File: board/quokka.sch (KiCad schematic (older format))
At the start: 0 parts

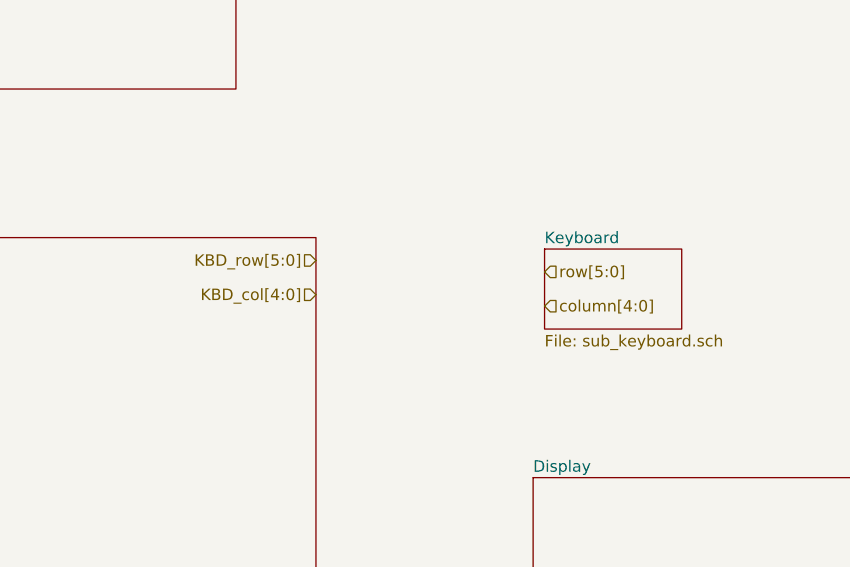
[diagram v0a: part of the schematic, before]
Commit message: Added some buttons
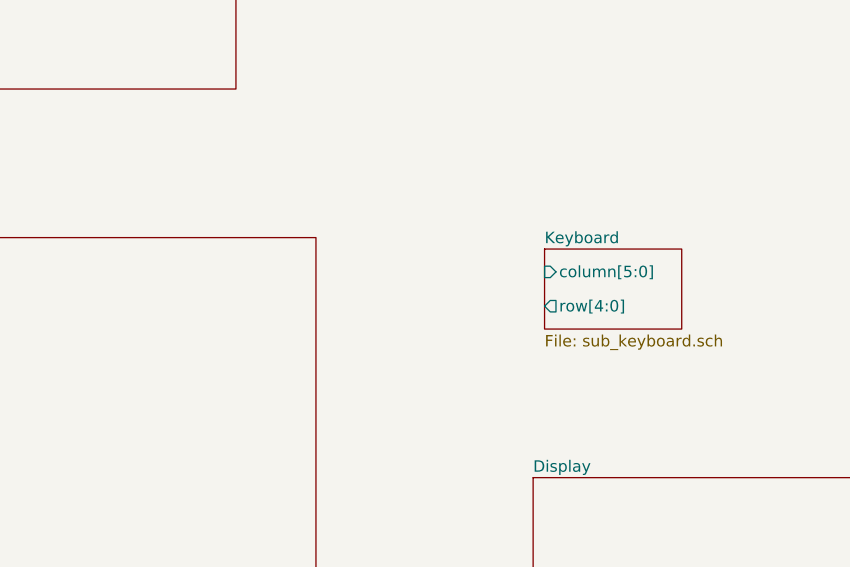
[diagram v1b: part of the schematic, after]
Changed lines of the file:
@@
 EESchema Schematic File Version 4
+LIBS:quokka-cache
 EELAYER 26 0
 EELAYER END
 $Descr A4 11693 8268
 encoding utf-8
-Sheet 1 7
+Sheet 1 8
 Title ""
 Date ""
@@
 F0 "Keyboard" 50
 F1 "sub_keyboard.sch" 50
+F2 "column[5:0]" I L 8400 3750 50
+F3 "row[4:0]" O L 8400 3900 50
 $EndSheet
-Text HLabel 8400 3750 2    50   Input ~ 0
-row[5:0]
-Text HLabel 8400 3900 2    50   Input ~ 0
-column[4:0]
-Text HLabel 7400 3700 0    50   Input ~ 0
-KBD_row[5:0]
-Text HLabel 7400 3850 0    50   Input ~ 0
-KBD_col[4:0]
 $EndSCHEMATC

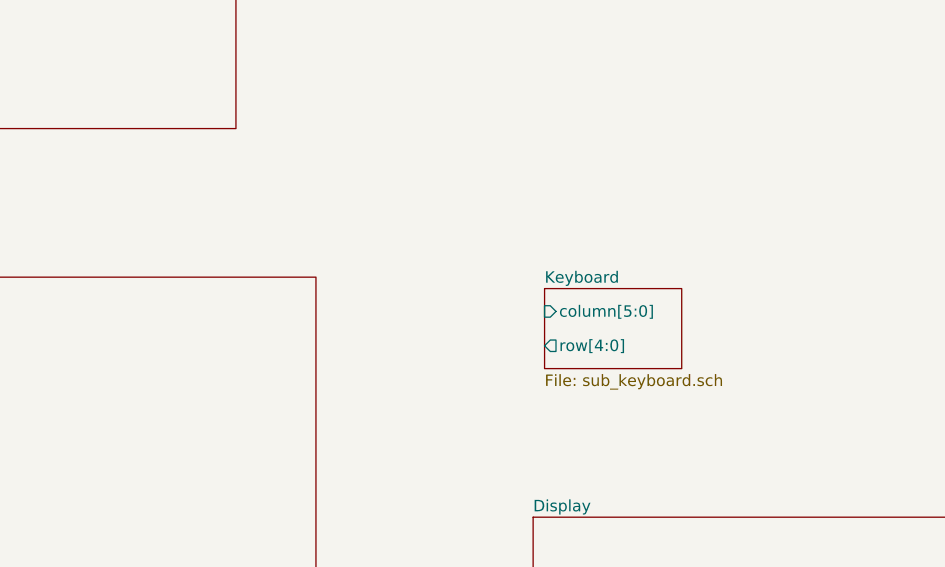
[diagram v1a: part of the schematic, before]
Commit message: Updated keyboard
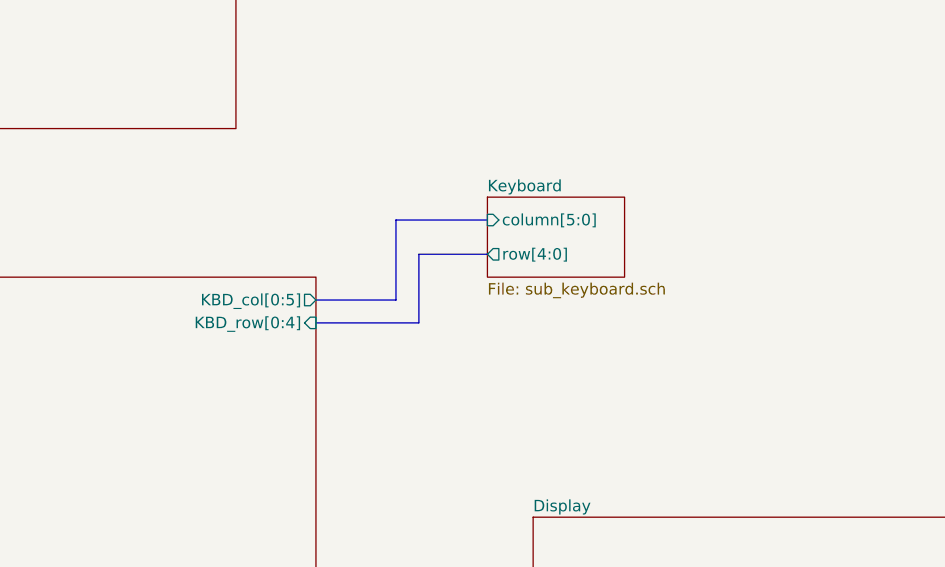
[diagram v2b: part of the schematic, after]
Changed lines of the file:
@@
 F0 "FPGA" 50
 F1 "sub_fpga.sch" 50
+F2 "KBD_col[0:5]" O R 7400 3700 50
+F3 "KBD_row[0:4]" I R 7400 3800 50
 $EndSheet
 $Sheet
@@
 $EndSheet
 $Sheet
-S 8400 3650 600  350
+S 8150 3250 600  350
 U 5A9C1519
 F0 "Keyboard" 50
 F1 "sub_keyboard.sch" 50
-F2 "column[5:0]" I L 8400 3750 50
-F3 "row[4:0]" O L 8400 3900 50
+F2 "column[5:0]" I L 8150 3350 50
+F3 "row[4:0]" O L 8150 3500 50
 $EndSheet
+Wire Bus Line
+	7400 3700 7750 3700
+Wire Bus Line
+	7750 3700 7750 3350
+Wire Bus Line
+	7750 3350 8150 3350
+Wire Bus Line
+	7850 3500 7850 3800
+Wire Bus Line
+	7850 3800 7400 3800
+Wire Bus Line
+	8150 3500 7850 3500
 $EndSCHEMATC

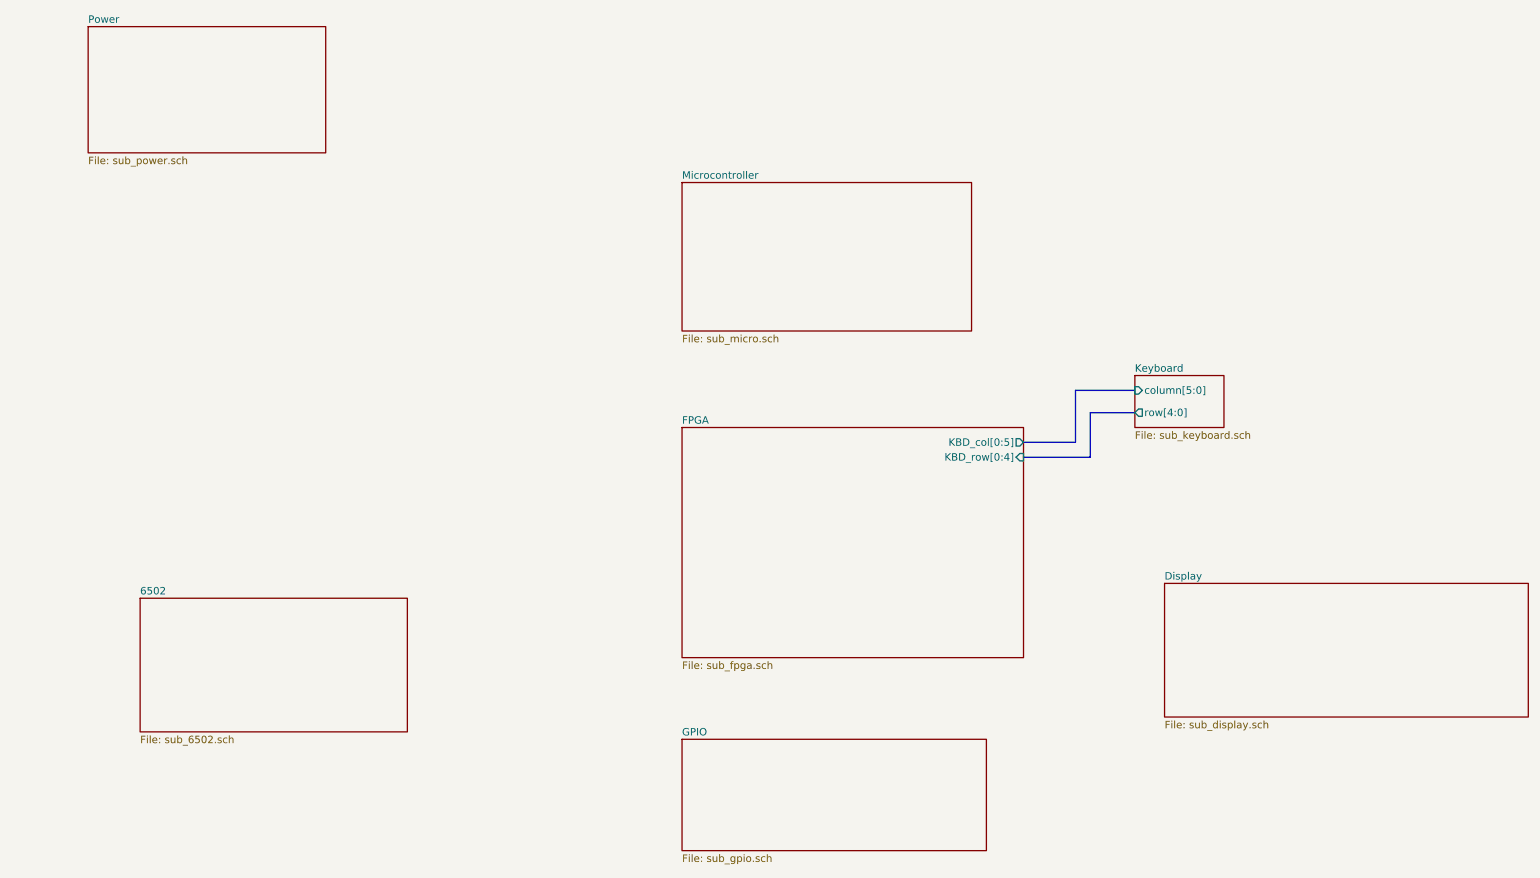
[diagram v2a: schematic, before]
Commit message: More progress on the schematic. 6502 Done.
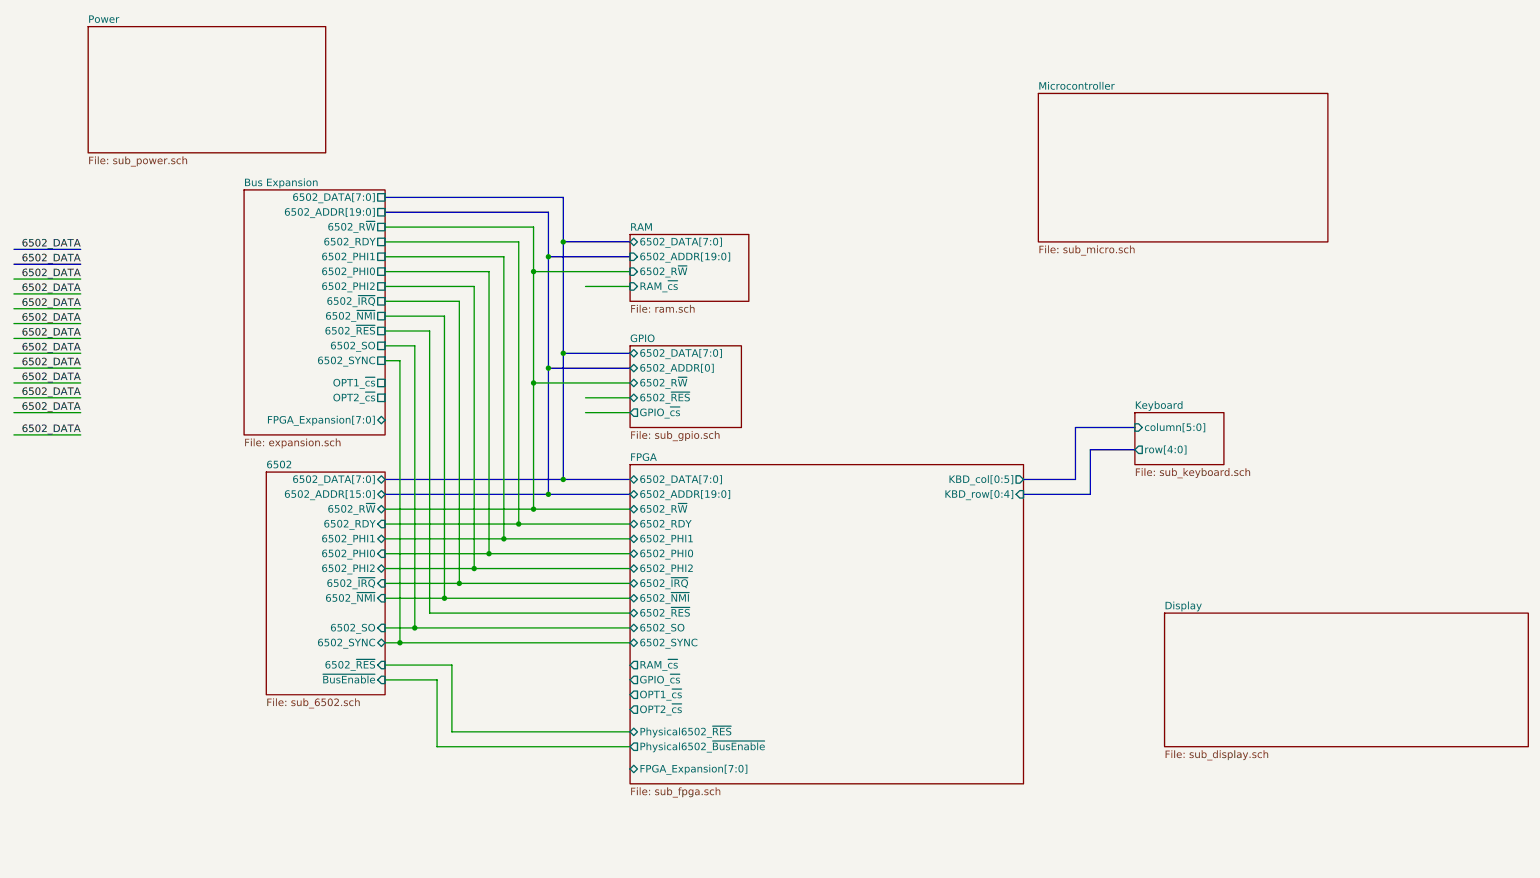
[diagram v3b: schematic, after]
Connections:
- net labels added: 6502_DATA
- wire segments 0 -> 63

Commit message: More schematic progress
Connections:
- net labels removed: 6502_DATA
- wire segments 63 -> 57

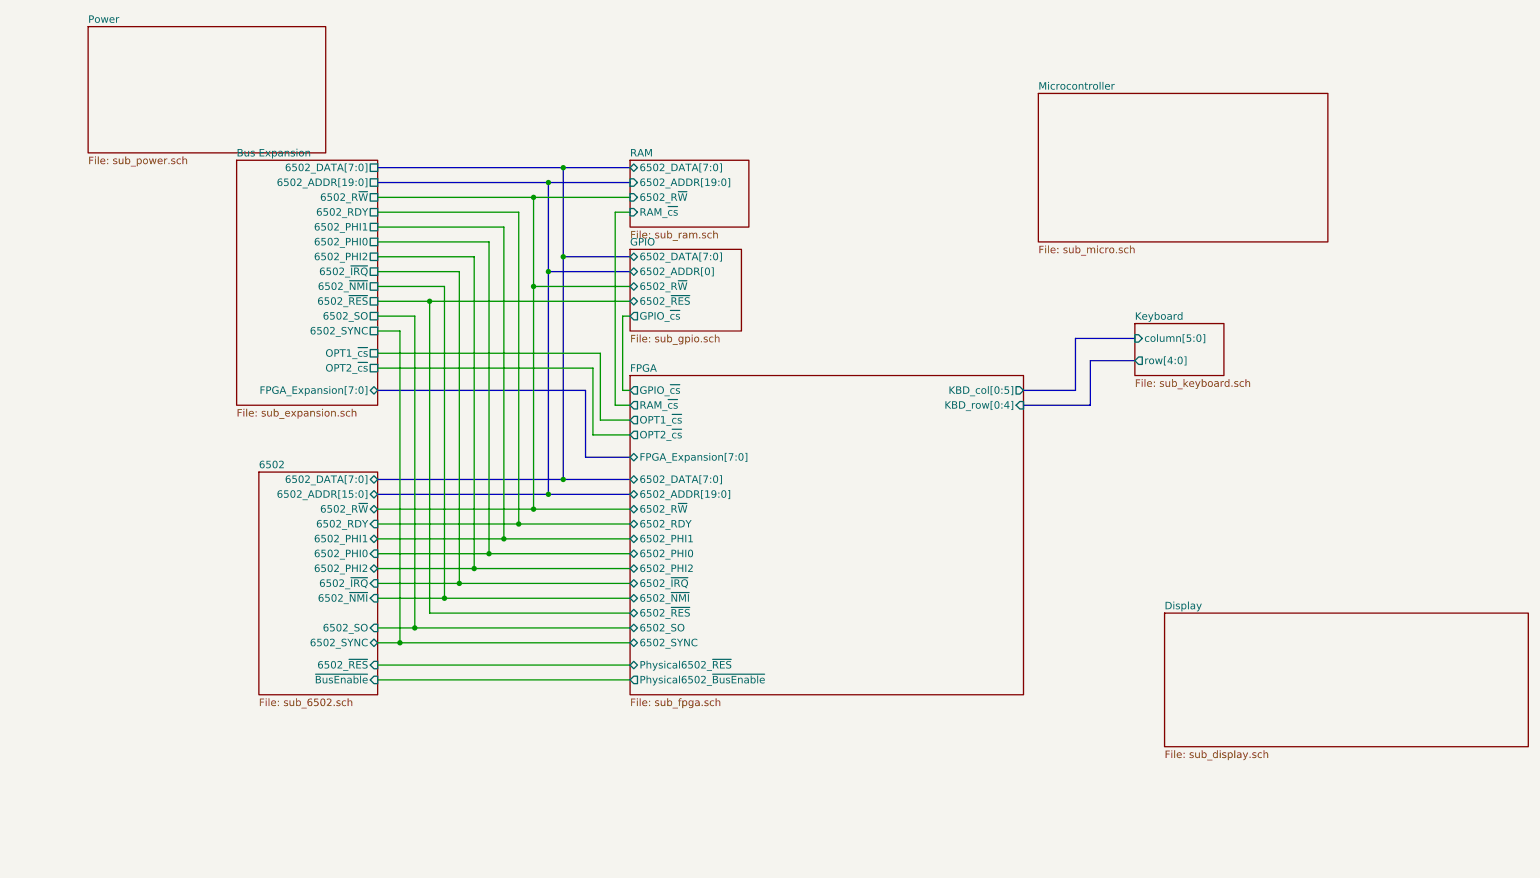
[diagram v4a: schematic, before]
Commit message: Level converters complete, display almost done
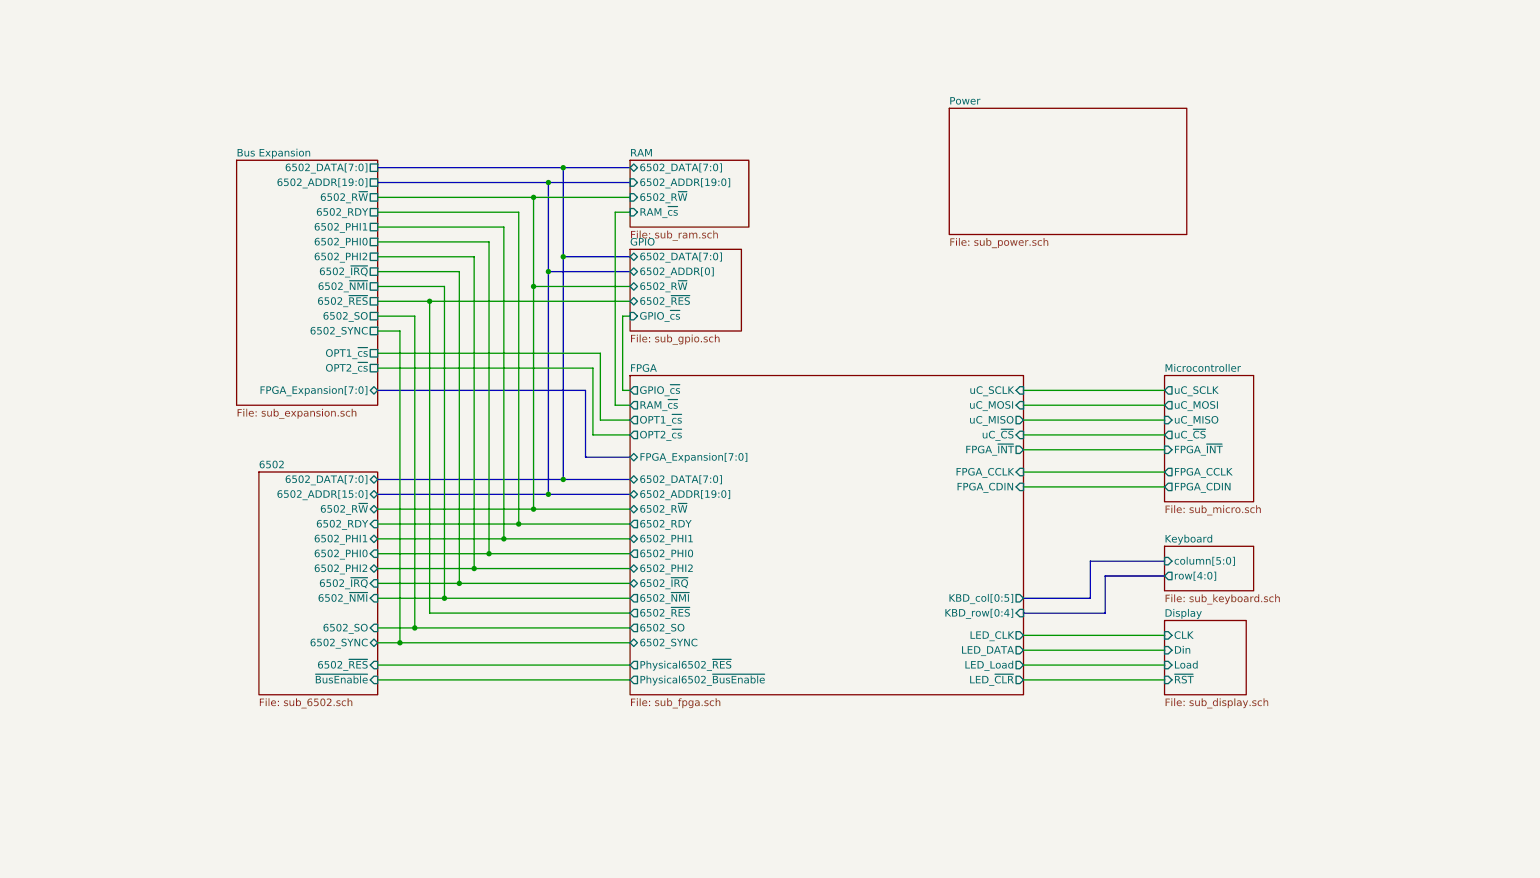
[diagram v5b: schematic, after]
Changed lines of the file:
@@
 EELAYER 26 0
 EELAYER END
-$Descr A4 11693 8268
+$Descr USLetter 11000 8500
 encoding utf-8
-Sheet 1 10
+Sheet 1 15
 Title ""
 Date ""
@@
 Comment2 ""
 Comment3 ""
-Comment4 ""
+Comment4 "Quokka 6502 Microprocessor Trainer"
 $EndDescr
 $Sheet
-S 1100 900  1600 850
+S 6900 1450 1600 850
 U 5A9C14CE
 F0 "Power" 50
@@
 $EndSheet
 $Sheet
-S 7500 1350 1950 1000
+S 8350 3250 600  850
 U 5A9C14E5
 F0 "Microcontroller" 50
 F1 "sub_micro.sch" 50
+F2 "uC_SCLK" O L 8350 3350 50
+F3 "uC_MOSI" O L 8350 3450 50
+F4 "uC_MISO" I L 8350 3550 50
+F5 "uC_~CS" O L 8350 3650 50
+F6 "FPGA_~INT" I L 8350 3750 50
+F7 "FPGA_CCLK" O L 8350 3900 50
+F8 "FPGA_CDIN" O L 8350 4000 50
 $EndSheet
 $Sheet
@@
 F3 "6502_R~W" B L 4750 2650 50
 F4 "6502_ADDR[0]" B L 4750 2550 50
-F5 "GPIO_~cs" O L 4750 2850 50
+F5 "GPIO_~cs" I L 4750 2850 50
 F6 "6502_~RES" B L 4750 2750 50
 $EndSheet
 $Sheet
-S 8350 4850 2450 900
+S 8350 4900 550  500
 U 5A9C150A
 F0 "Display" 50
 F1 "sub_display.sch" 50
-$EndSheet
-$Sheet
-S 8150 2900 600  350
+F2 "CLK" I L 8350 5000 50
+F3 "~RST" I L 8350 5300 50
+F4 "Load" I L 8350 5200 50
+F5 "Din" I L 8350 5100 50
+$EndSheet
+$Sheet
+S 8350 4400 600  300
 U 5A9C1519
 F0 "Keyboard" 50
 F1 "sub_keyboard.sch" 50
-F2 "column[5:0]" I L 8150 3000 50
-F3 "row[4:0]" O L 8150 3150 50
-$EndSheet
-Wire Bus Line
-	7400 3350 7750 3350
-Wire Bus Line
-	7750 3350 7750 3000
-Wire Bus Line
-	7750 3000 8150 3000
-Wire Bus Line
-	7850 3150 7850 3450
-Wire Bus Line
-	7850 3450 7400 3450
-Wire Bus Line
-	8150 3150 7850 3150
+F2 "column[5:0]" I L 8350 4500 50
+F3 "row[4:0]" O L 8350 4600 50
+$EndSheet
 $Sheet
 S 2100 1800 950  1650
@@
 $EndSheet
 $Sheet
-S 4750 3250 2650 2150
-U 5A9C14F1
-F0 "FPGA" 50
-F1 "sub_fpga.sch" 50
-F2 "KBD_col[0:5]" O R 7400 3350 50
-F3 "KBD_row[0:4]" I R 7400 3450 50
-F4 "6502_DATA[7:0]" T L 4750 3950 50
-F5 "6502_RDY" B L 4750 4250 50
-F6 "6502_PHI1" B L 4750 4350 50
-F7 "6502_PHI0" B L 4750 4450 50
-F8 "6502_PHI2" B L 4750 4550 50
-F9 "6502_SO" B L 4750 4950 50
-F10 "6502_ADDR[19:0]" B L 4750 4050 50
-F11 "6502_R~W" B L 4750 4150 50
-F12 "6502_~IRQ" B L 4750 4650 50
-F13 "6502_~NMI" B L 4750 4750 50
-F14 "6502_~RES" B L 4750 4850 50
-F15 "RAM_~cs" O L 4750 3450 50
-F16 "GPIO_~cs" O L 4750 3350 50
-F17 "OPT1_~cs" O L 4750 3550 50
-F18 "OPT2_~cs" O L 4750 3650 50
-F19 "6502_SYNC" B L 4750 5050 50
-F20 "Physical6502_~RES" B L 4750 5200 50
-F21 "Physical6502_~BusEnable" O L 4750 5300 50
-F22 "FPGA_Expansion[7:0]" B L 4750 3800 50
-$EndSheet
-$Sheet
 S 2250 3900 800  1500
 U 5A9C14D9
@@
 Wire Bus Line
 	3050 3350 4450 3350
+$Sheet
+S 4750 3250 2650 2150
+U 5A9C14F1
+F0 "FPGA" 50
+F1 "sub_fpga.sch" 50
+F2 "KBD_col[0:5]" O R 7400 4750 50
+F3 "KBD_row[0:4]" I R 7400 4850 50
+F4 "6502_DATA[7:0]" T L 4750 3950 50
+F5 "6502_ADDR[19:0]" B L 4750 4050 50
+F6 "RAM_~cs" O L 4750 3450 50
+F7 "GPIO_~cs" O L 4750 3350 50
+F8 "OPT1_~cs" O L 4750 3550 50
+F9 "OPT2_~cs" O L 4750 3650 50
+F10 "FPGA_Expansion[7:0]" B L 4750 3800 50
+F11 "LED_CLK" O R 7400 5000 50
+F12 "LED_DATA" O R 7400 5100 50
+F13 "LED_Load" O R 7400 5200 50
+F14 "6502_R~W" B L 4750 4150 50
+F15 "6502_RDY" O L 4750 4250 50
+F16 "6502_PHI1" B L 4750 4350 50
+F17 "6502_PHI0" O L 4750 4450 50
+F18 "6502_PHI2" B L 4750 4550 50
+F19 "6502_~IRQ" B L 4750 4650 50
+F20 "6502_~NMI" O L 4750 4750 50
+F21 "Physical6502_~RES" O L 4750 5200 50
+F22 "6502_SO" O L 4750 4950 50
+F23 "6502_SYNC" B L 4750 5050 50
+F24 "6502_~RES" O L 4750 4850 50
+F25 "Physical6502_~BusEnable" O L 4750 5300 50
+F26 "uC_SCLK" I R 7400 3350 50
+F27 "uC_MOSI" I R 7400 3450 50
+F28 "uC_MISO" O R 7400 3550 50
+F29 "uC_~CS" I R 7400 3650 50
+F30 "FPGA_~INT" O R 7400 3750 50
+F31 "FPGA_CCLK" I R 7400 3900 50
+F32 "FPGA_CDIN" I R 7400 4000 50
+F33 "LED_~CLR" O R 7400 5300 50
+$EndSheet
+Wire Wire Line
+	8350 3350 7400 3350
+Wire Wire Line
+	7400 3450 8350 3450
+Wire Wire Line
+	8350 3550 7400 3550
+Wire Wire Line
+	7400 3650 8350 3650
+Wire Wire Line
+	8350 3750 7400 3750
+Wire Wire Line
+	7400 3900 8350 3900
+Wire Wire Line
+	8350 4000 7400 4000
+Wire Bus Line
+	7950 4600 7950 4850
+Wire Bus Line
+	7950 4850 7400 4850
+Wire Bus Line
+	7950 4600 8350 4600
+Wire Bus Line
+	7400 4750 7850 4750
+Wire Bus Line
+	7850 4750 7850 4500
+Wire Bus Line
+	7850 4500 8350 4500
+Wire Wire Line
+	8350 5000 7400 5000
+Wire Wire Line
+	7400 5100 8350 5100
+Wire Wire Line
+	8350 5200 7400 5200
+Wire Wire Line
+	7400 5300 8350 5300
 $EndSCHEMATC
